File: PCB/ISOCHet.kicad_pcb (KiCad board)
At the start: 2 copper layers, 57.1 x 38.1 mm, 19 parts, among them J1 USB_C_Receptacle_USB2.0, J2 Conn_01x08_Pin, SW0 BOOT, SW1 TAB, SW2 ENTER, SW3 CAPS, SW4 CAPS_STEP1.5, SW5 CAPS_STEP1.25, U1 CH552G, U2 USBLC6-2P6

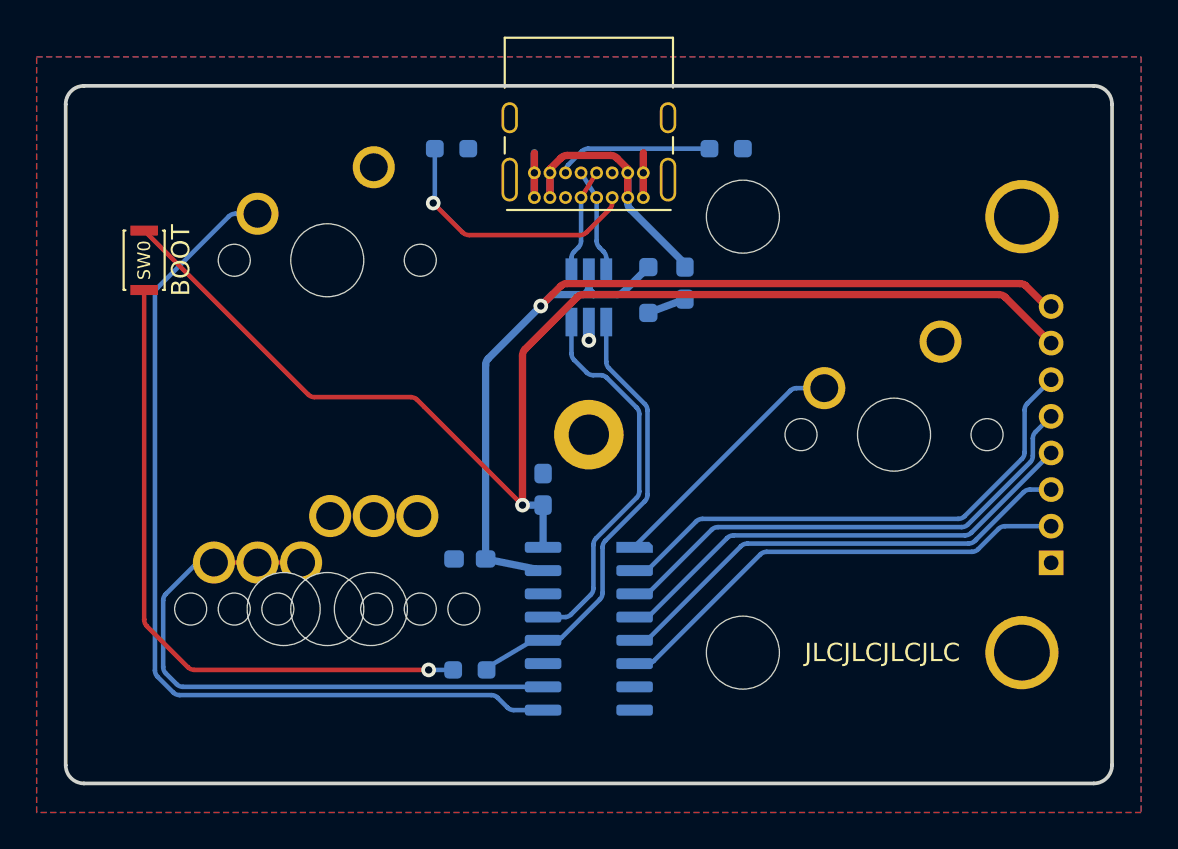
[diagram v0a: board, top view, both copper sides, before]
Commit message: Tweak ESD routing
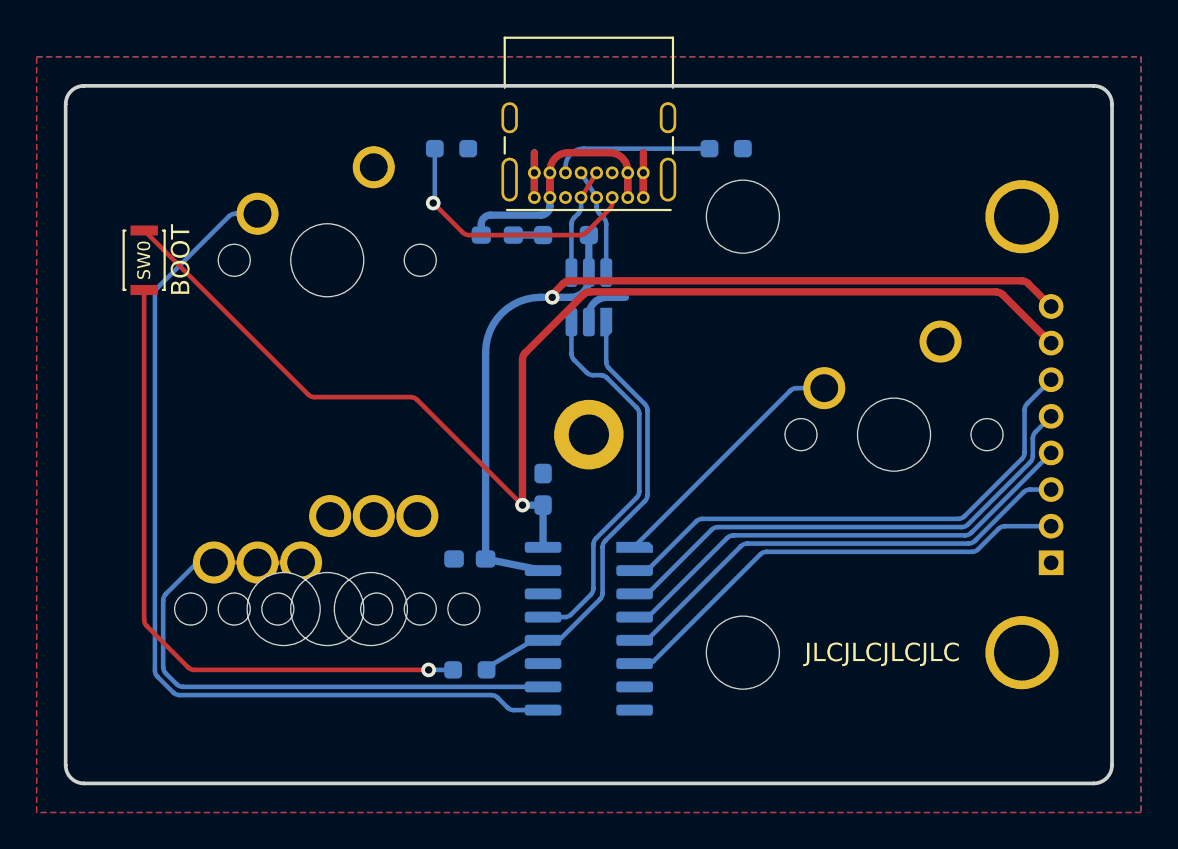
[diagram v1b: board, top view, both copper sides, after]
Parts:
- moved F1 10.6 mm to (153.8, 46.2), turned to 0 degrees
- moved D1 5.41 mm to (157.5, 46.2), turned to 180 degrees
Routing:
- net VCC: track 56.2 -> 52.9 mm
- net GND: track 8.68 -> 11.9 mm, vias 1 -> 0
- net VBUS: track 15.5 -> 16.2 mm
- net Net-(D1-A): track 2.14 -> 1.62 mm

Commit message: Use Alps SKQG switch for BOOT, update LCSC part numbers, add DigiKey part numbers
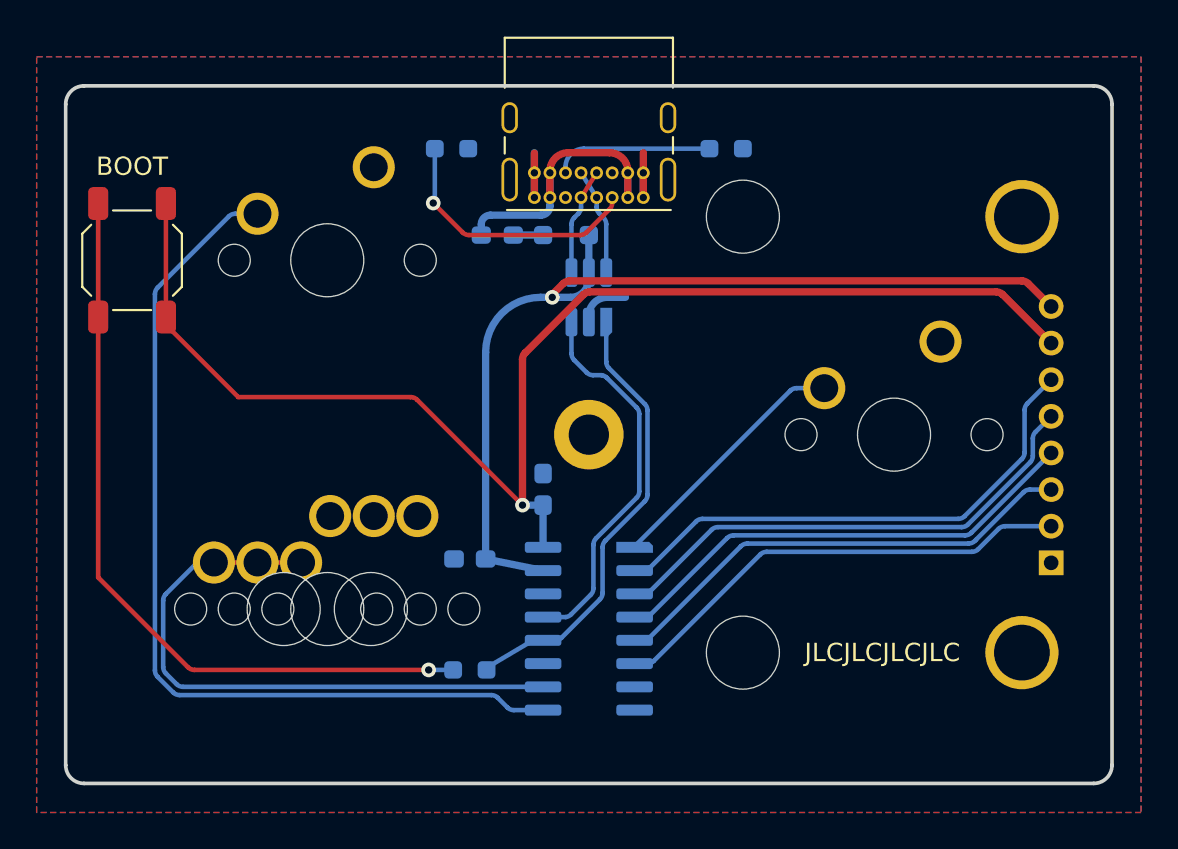
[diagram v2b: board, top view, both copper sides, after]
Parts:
- SW0: footprint Button_Switch_SMD:SW_SPST_CK_KXT3 -> Button_Switch_SMD:SW_SPST_SKQG_WithStem
- moved SW0 0.66 mm to (133.8, 47.6)
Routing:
- net Net-(R3-Pad2): track 36.0 -> 41.8 mm
- net +3V3: track 69.8 -> 73.2 mm

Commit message: Change footprint for USB port
USB C socket is now GSB1C211110DS1HR instead of GCT USB4085. Update routing with more filleting on 90° corners.
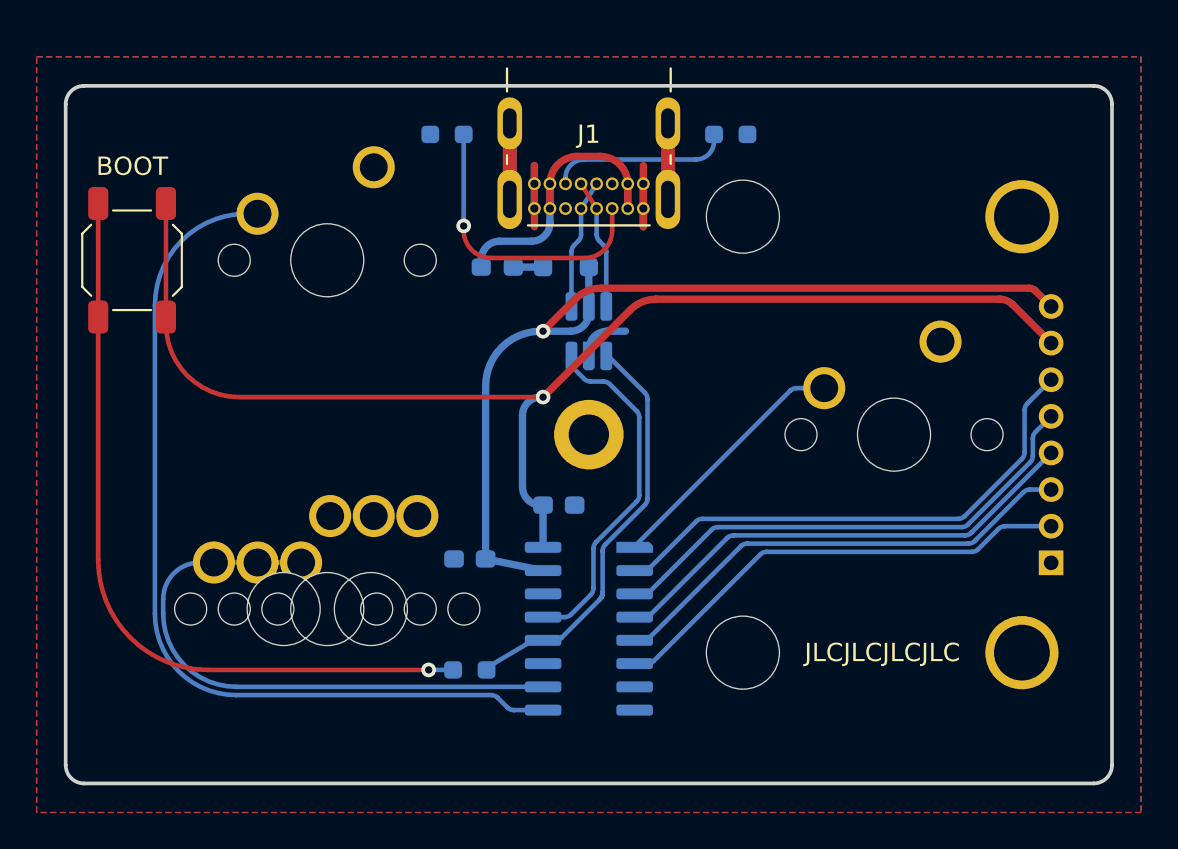
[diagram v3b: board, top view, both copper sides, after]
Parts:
- J1: footprint Connector_USB:USB_C_Receptacle_GCT_USB4085 -> Project Library:GSB1C211110DS1HR
- moved J1 4.56 mm to (158.8, 40.8)
- moved U2 1.85 mm to (158.8, 51.5)
- moved D1 1.75 mm to (157.5, 48.0)
- moved F1 1.75 mm to (153.8, 48.0)
- moved C2 1.22 mm to (157.1, 61.0), turned to 0 degrees
- moved R1 0.82 mm to (151.0, 40.8), turned to 180 degrees
- moved R2 0.82 mm to (166.5, 40.8)
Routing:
- net GND: track 11.9 -> 26.4 mm
- net +3V3: track 73.2 -> 69.8 mm
- net UDP: track 24.0 -> 22.2 mm
- net UDM: track 20.9 -> 19.2 mm
- net Net-(J1-CC1): track 14.6 -> 16.2 mm
- net VCC: track 52.9 -> 51.6 mm
- net P_DP: track 5.86 -> 7.11 mm
- net P_DM: track 5.86 -> 7.11 mm
- net Tab: track 50.2 -> 49.0 mm
- net Net-(J1-CC2): track 8.71 -> 9.87 mm
- net VBUS: track 16.2 -> 17.3 mm

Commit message: Swap R1 and R2 (again)
Also, make some routing prettier.
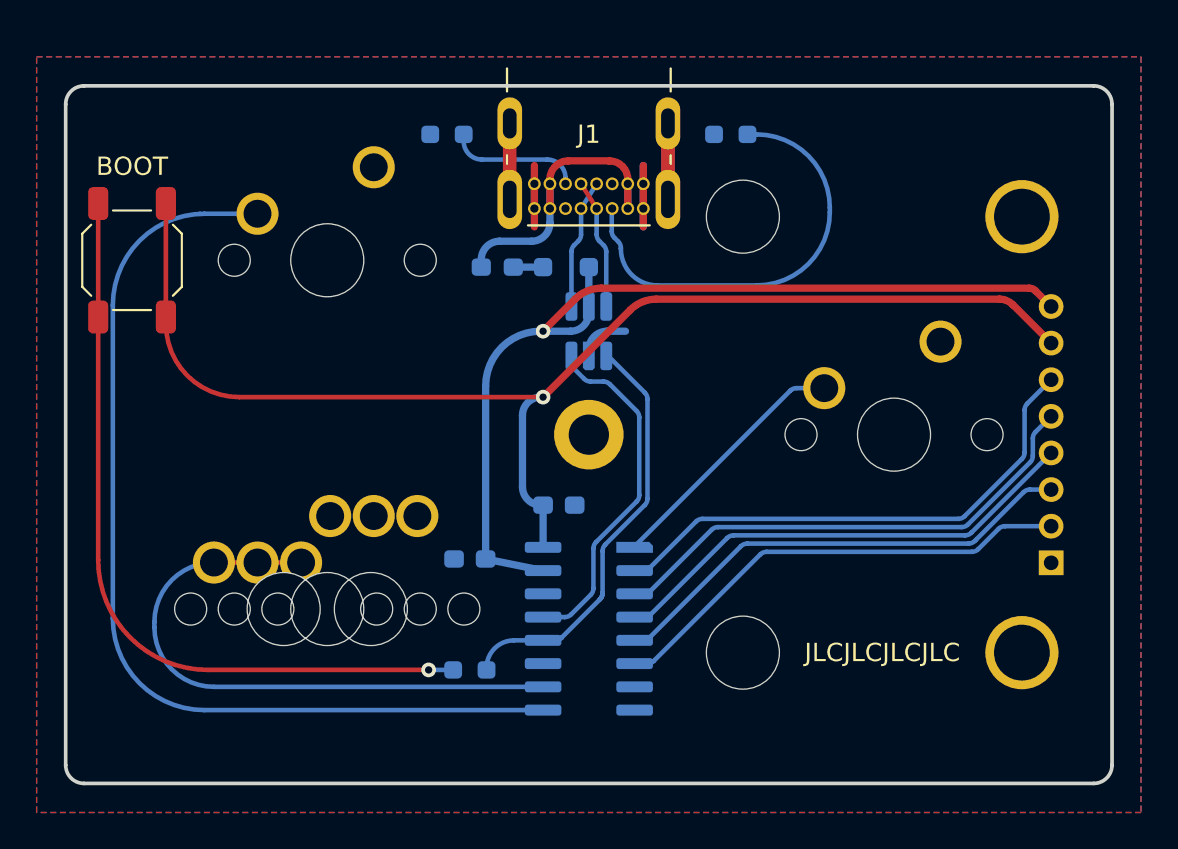
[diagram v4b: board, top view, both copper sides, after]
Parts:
- turned R1 to 180 degrees
- renumbered R2 to R1, R1 to R2
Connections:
- R1 pad 1: Net-(J1-CC2) -> Net-(J1-CC1)
- R2 pad 1: Net-(J1-CC1) -> Net-(J1-CC2)
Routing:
- net Net-(J1-CC1): track 16.2 -> 23.8 mm, vias 1 -> 0
- net Tab: track 49.0 -> 53.8 mm
- net Net-(J1-CC2): track 9.87 -> 7.32 mm
- net Caps: track 32.3 -> 33.8 mm
- net UDP: track 22.2 -> 23.3 mm

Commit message: Refresh from schematic and tweak routing
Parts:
- moved C1 0.36 mm to (152.2, 64.3)
- moved U1 0.28 mm to (158.8, 67.5)
- moved C2 0.20 mm to (157.1, 60.8)
- moved R3 0.20 mm to (152.2, 69.8)
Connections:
- net Net-(J2-Pin_2) renamed RST
- net Net-(J2-Pin_3) renamed P17
- net Net-(J2-Pin_4) renamed P16
- net Net-(J2-Pin_5) renamed P15
- net Net-(J2-Pin_6) renamed P14
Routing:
- net Tab: track 53.8 -> 55.8 mm
- net P15: track 27.4 -> 26.4 mm
- net +3V3: track 69.8 -> 68.9 mm
- net P14: track 28.5 -> 27.6 mm
- net RST: track 25.8 -> 24.8 mm
- net P17: track 26.1 -> 25.1 mm
- net Enter: track 14.0 -> 13.1 mm
- net UDP: track 23.3 -> 22.6 mm
- net P16: track 26.4 -> 25.7 mm
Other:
- board text added: "P14"
- board text added: "P15"
- board text added: "P16"
- board text added: "P17"
- board text added: "RST"
- board text removed: "1.4"
- board text removed: "1.5"
- board text removed: "1.6"
- board text removed: "3.0"
- board text removed: "3.1"

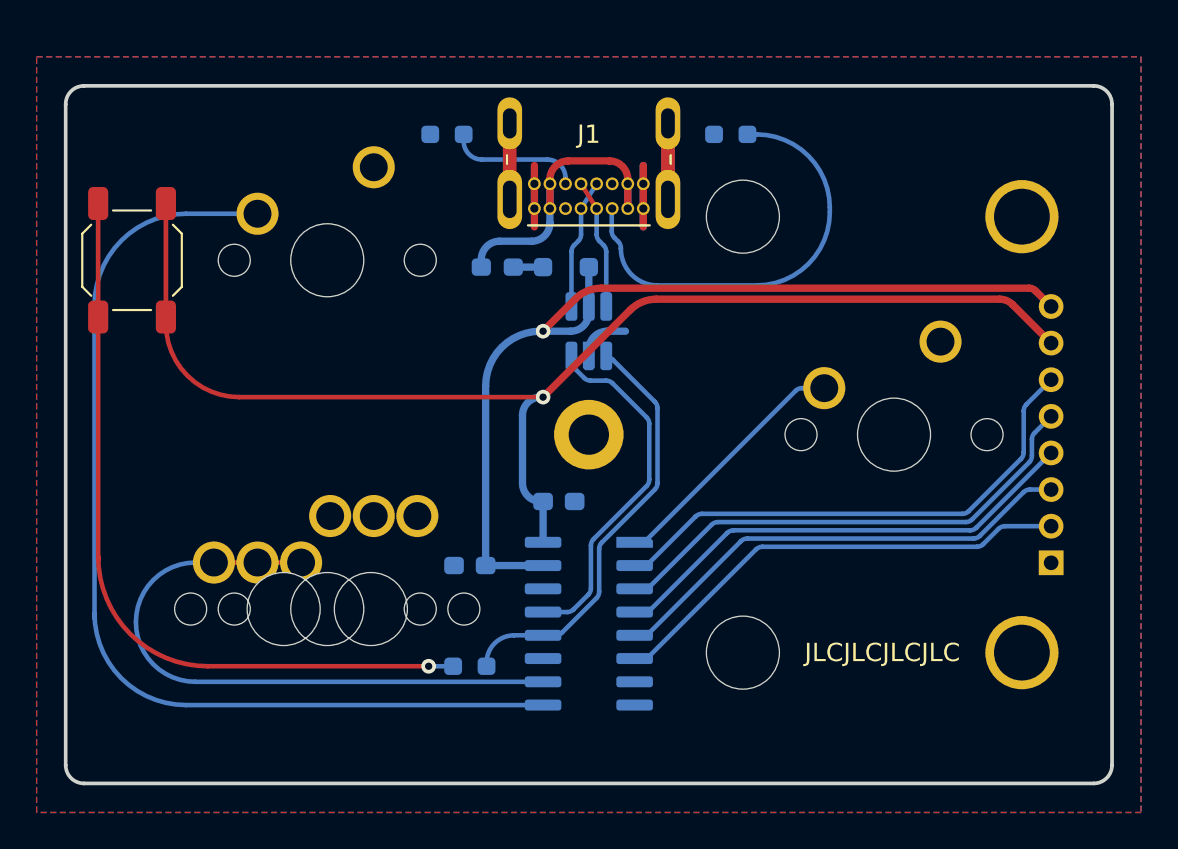
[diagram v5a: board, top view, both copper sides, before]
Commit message: Rotated CH552 90° and rerouted accordingly
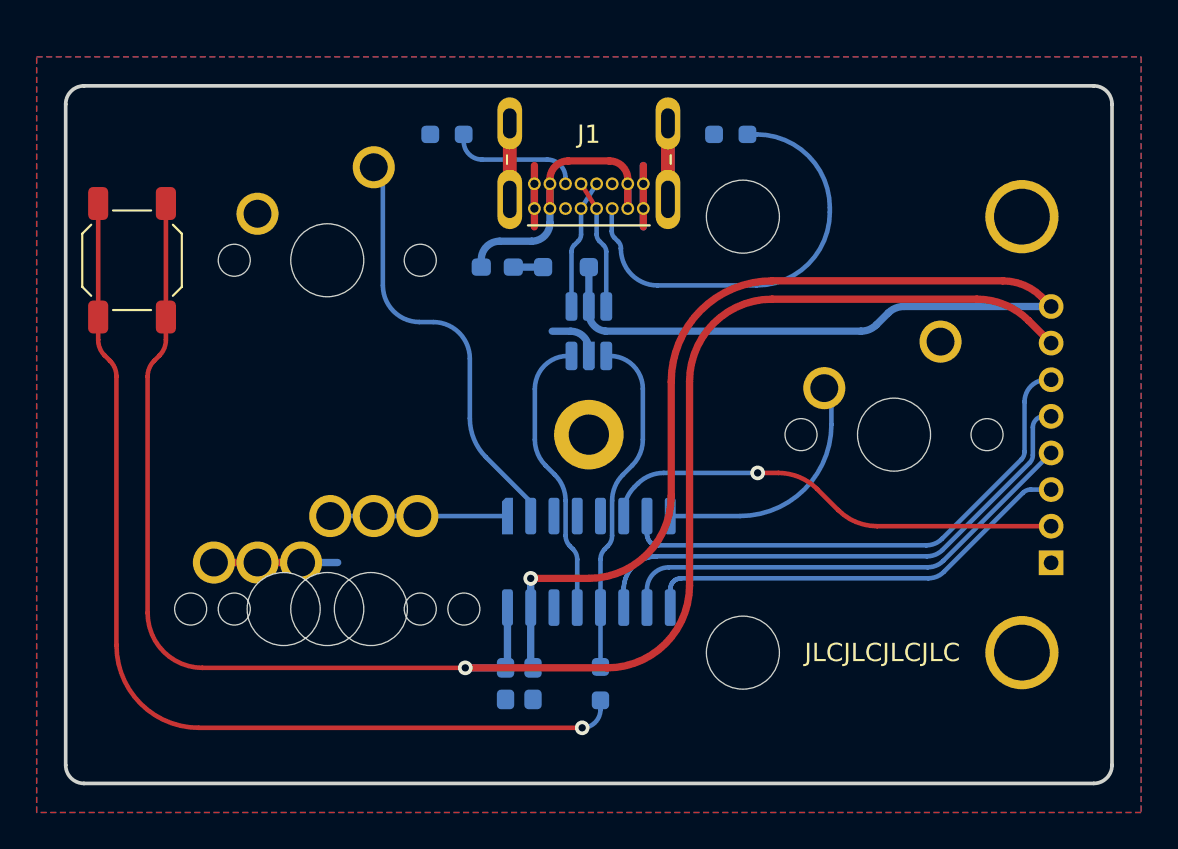
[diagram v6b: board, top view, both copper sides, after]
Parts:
- moved C2 10.4 mm to (154.2, 70.8), turned to -90 degrees
- moved C1 7.31 mm to (155.7, 70.8), turned to -90 degrees
- moved R3 7.20 mm to (159.4, 70.8), turned to -90 degrees
- moved U1 3.38 mm to (158.8, 64.1), turned to -90 degrees
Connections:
- J2 pad 3: P17 -> P11
- J2 pad 4: P16 -> P33
- J2 pad 5: P15 -> P34
- J2 pad 6: P14 -> P31
- SW1 pad 1: Tab -> GND
- SW1 pad 2: GND -> Tab
- SW3 pad 1: Caps -> GND
- SW3 pad 2: GND -> Caps
- SW4 pad 1: Caps -> GND
- SW4 pad 2: GND -> Caps
- SW5 pad 1: Caps -> GND
- SW5 pad 2: GND -> Caps
- U1 pad 1: Enter -> Caps
- U1 pad 10: Caps -> P33
- U1 pad 11: unconnected-(U1-P3.4-Pad11) -> P34
- U1 pad 2: P14 -> Tab
- U1 pad 3: P15 -> unconnected-(U1-P1.5-Pad3)
- U1 pad 4: P16 -> unconnected-(U1-P1.6-Pad4)
- U1 pad 5: P17 -> unconnected-(U1-P1.7-Pad5)
- U1 pad 7: unconnected-(U1-P3.1-Pad7) -> P31
- U1 pad 8: unconnected-(U1-P3.0-Pad8) -> Enter
- U1 pad 9: Tab -> P11
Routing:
- net Tab: track 55.8 -> 21.9 mm
- net P34: track 0.00 -> 29.2 mm
- net P31: track 0.00 -> 28.7 mm
- net P14: track 27.6 -> 0.00 mm
- net +3V3: track 68.9 -> 95.5 mm
- net P15: track 26.4 -> 0.00 mm
- net P33: track 0.00 -> 26.2 mm
- net P16: track 25.7 -> 0.00 mm
- net P17: track 25.1 -> 0.00 mm
- net P11: track 0.00 -> 24.1 mm
- net Caps: track 33.7 -> 9.68 mm
- net VCC: track 51.9 -> 73.5 mm
- net Net-(R3-Pad2): track 42.0 -> 54.3 mm
- net GND: track 26.4 -> 37.9 mm
- net UDP: track 22.6 -> 18.6 mm
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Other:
- board text added: "P11"
- board text added: "P31"
- board text added: "P33"
- board text added: "P34"
- board text removed: "P14"
- board text removed: "P15"
- board text removed: "P16"
- board text removed: "P17"
